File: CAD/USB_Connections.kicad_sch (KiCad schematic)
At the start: 14 parts, among them J6 USB_C_Plug_USB2.0, J7 USB_C_Plug_USB2.0

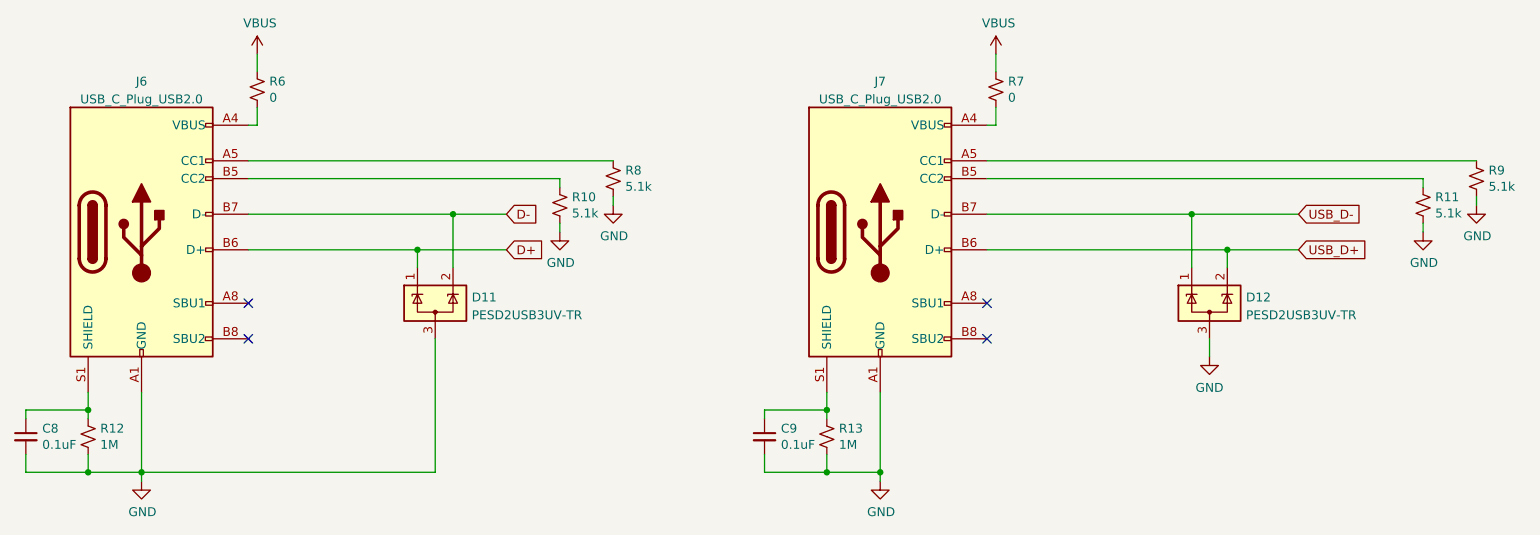
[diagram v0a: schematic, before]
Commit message: Remove unused USB from schematic
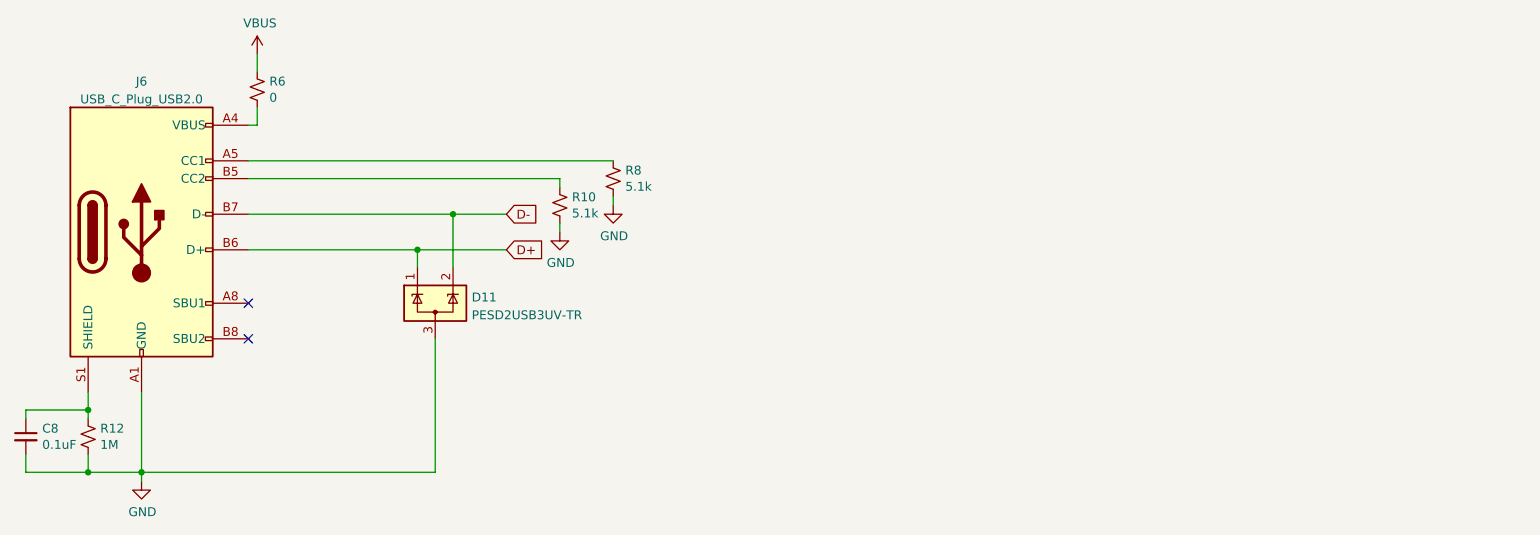
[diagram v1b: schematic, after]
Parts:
- removed C9: 0.1uF, BadgePirates:C_0805_2012Metric, symbol Device:C_Small
- removed D12: PESD2USB3UV-TR, Package_TO_SOT_SMD:SOT-23, symbol BadgePiratesSymbolLibrary:PESD2USB3UV-TR
- removed J7: USB_C_Plug_USB2.0, BadgePirates:USB_C_Receptical-Jing, symbol BadgePiratesSymbolLibrary:USB_C_Plug_USB2.0
- removed R11, R9: 5.1k, BadgePirates:R_1206_3216Metric, symbol Device:R_Small_US
- removed R13: 1M, BadgePirates:R_1206_3216Metric, symbol Device:R_Small_US
- removed R7: 0, BadgePirates:R_1206_3216Metric, symbol Device:R_Small_US
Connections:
- no-connect marks 4 -> 2
